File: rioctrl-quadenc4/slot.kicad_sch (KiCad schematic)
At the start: 5 parts, among them J2 Conn_02x13_Odd_Even

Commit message: Fix ERC, add title information to sch, add initial version of build scripts
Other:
- company: (none) -> R. Veips
- title: (none) -> rioctrl-quadenc4
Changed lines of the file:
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@@
 	(generator_version "8.0")
 	(paper "A4")
+	(title_block
+		(title "rioctrl-quadenc4")
+		(date "2024-08-25")
+		(rev "${VERSION}")
+		(company "R. Veips")
+	)
 	(junction
 		(at 154.94 87.63)

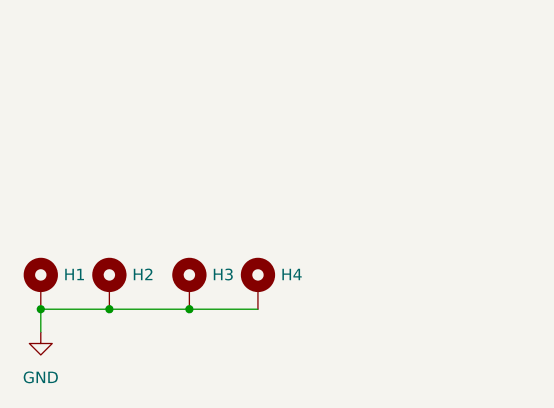
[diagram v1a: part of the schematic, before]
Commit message: Fill in BOM (LCSC#)
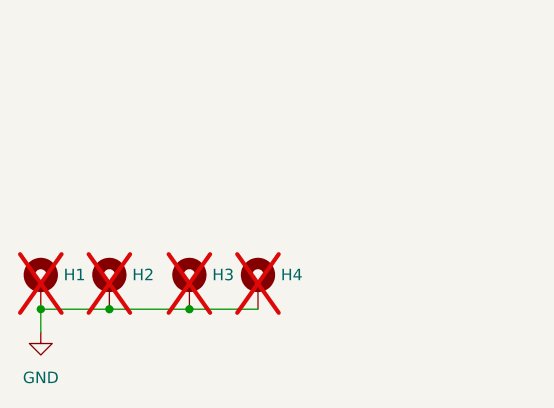
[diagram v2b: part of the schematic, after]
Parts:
- H1, H2, H3, H4: now not fitted
- J2: LCSC# (none) -> C2894993
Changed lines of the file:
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@@
+			)
+		)
+		(property "LCSC#" "C2894993"
+			(at 133.35 80.01 0)
+			(effects
+				(font
+					(size 1.27 1.27)
+				)
+				(hide yes)
 			)
 		)
@@
 		(in_bom no)
 		(on_board yes)
-		(dnp no)
+		(dnp yes)
 		(fields_autoplaced yes)
 		(property "Reference" "H2"
@@
 		(in_bom no)
 		(on_board yes)
-		(dnp no)
+		(dnp yes)
 		(fields_autoplaced yes)
 		(property "Reference" "H3"
@@
 		(in_bom no)
 		(on_board yes)
-		(dnp no)
+		(dnp yes)
 		(fields_autoplaced yes)
 		(property "Reference" "H4"
@@
 		(in_bom no)
 		(on_board yes)
-		(dnp no)
+		(dnp yes)
 		(fields_autoplaced yes)
 		(property "Reference" "H1"
